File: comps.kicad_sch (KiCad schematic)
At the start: 9 parts, among them J3 Micro_SD_Card_Det, U7 ICM-20608-G, U8 MMC5983MA

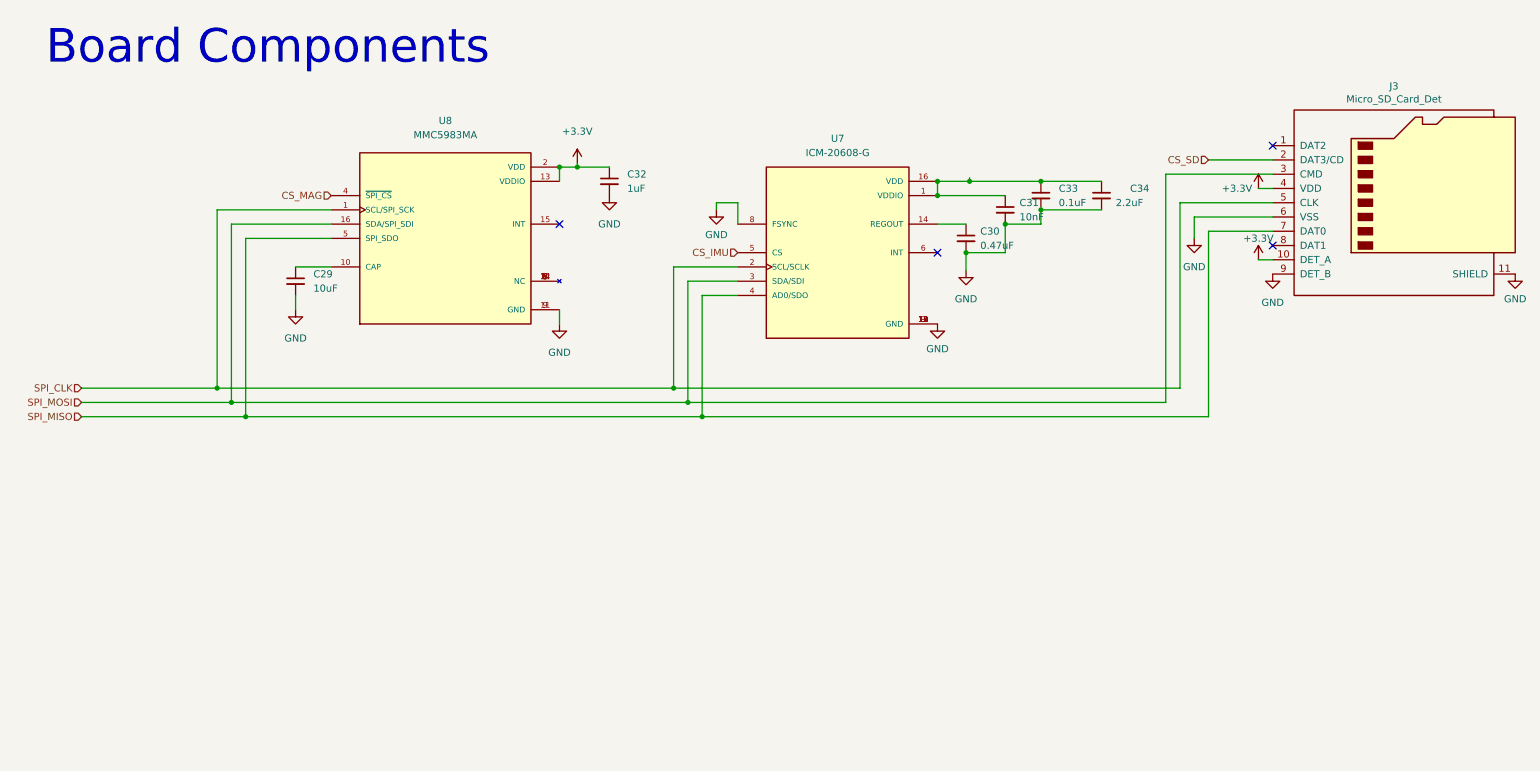
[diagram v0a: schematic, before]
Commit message: schematic review updated
fixed:
-pin 1 on the bootjumper is missing a connection. 
- Move the SD card to a 2nd SPI bus (so a 2nd set of MISO, MOSI, SCLK) as the rest of the bus is blocked while data is written to it, which would interrupt sensor readings. 
- Add a pull-up resistor on the DET_A pin of the micro SD card, and also connect that pin to the esp32 (picture from pickle) 
- VDD on the IMU (U7) is not connected to any power, should be connected to 3.3V 
- Turns out CAN capacitors C18, C19 actually aren’t needed. It’s up to you if you want to keep them, but if you do keep them could you change their value to “DNP” (stands for Do not place) 
-  Add test points to lines which can potentially cause issues. Most of the time this just means places that are connected to the ESP32, but especially places like the SPI lines (including chip selects). Also, add test points to TXD and RXD on the esp32 in case we have to solder to them for programming  

Servo Buck Converter 
- Pin 29 missing ground connection 
-  Add a text label with the part number of the 2.1uH inductor 

LTC4412s 
- No power net connected to Vin 
- stocky diodes replaced logic mosfets
- switched mosfets around so S is common
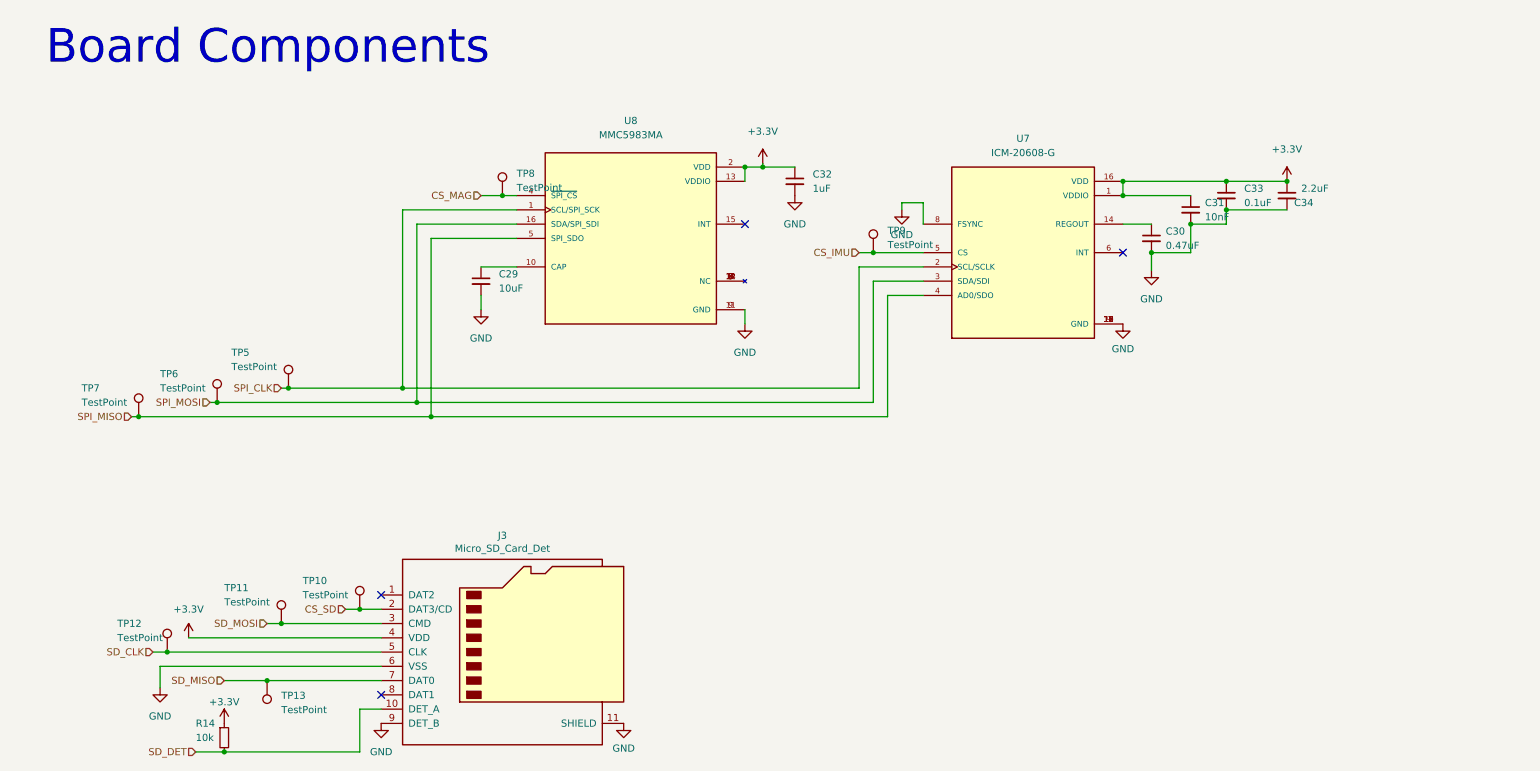
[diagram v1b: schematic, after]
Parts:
- added R14: 10k, symbol Device:R_Small
- added TP10, TP11, TP12, TP13, TP5, TP6, TP7, TP8, TP9: TestPoint, symbol Connector:TestPoint
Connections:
- net +3V3: now also C31.1, C33.1, C34.1, U7.1 (VDDIO), U7.16 (VDD), R14.1; no longer J3.10 (DET_A)
- net CS_IMU: now also TP9.1
- net CS_MAG: now also TP8.1
- net CS_SD: now also TP10.1
- net SPI_CLK: now also TP5.1; no longer J3.5 (CLK)
- net SPI_MISO: now also TP7.1; no longer J3.7 (DAT0)
- net SPI_MOSI: now also TP6.1; no longer J3.3 (CMD)
- new net SD_CLK: J3.5 (CLK), TP12.1
- new net SD_DET: J3.10 (DET_A), R14.2
- new net SD_MISO: J3.7 (DAT0), TP13.1
- new net SD_MOSI: J3.3 (CMD), TP11.1
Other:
- moved on the sheet: C29, C30, C31, C32, C33, C34, J3, U7, U8

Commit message: I don't want to lose all my changes so I will commit, commit.
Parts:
- R14: footprint (none) -> Resistor_SMD:R_0402_1005Metric
- TP10, TP11, TP12, TP13, TP5, TP6, TP7, TP8, TP9: footprint (none) -> TestPoint:TestPoint_Pad_D1.0mm
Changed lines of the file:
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@@
       (effects (font (size 1.27 1.27)) (justify left))
     )
-    (property "Footprint" "" (at 44.45 127 0)
+    (property "Footprint" "TestPoint:TestPoint_Pad_D1.0mm" (at 44.45 127 0)
       (effects (font (size 1.27 1.27)) hide)
     )
@@
       (effects (font (size 1.27 1.27)) (justify right))
     )
-    (property "Footprint" "" (at 52.07 132.08 0)
+    (property "Footprint" "TestPoint:TestPoint_Pad_D1.0mm" (at 52.07 132.08 0)
       (effects (font (size 1.27 1.27)) hide)
     )
@@
       (effects (font (size 1.27 1.27)) (justify left))
     )
-    (property "Footprint" "" (at 78.74 119.38 0)
+    (property "Footprint" "TestPoint:TestPoint_Pad_D1.0mm" (at 78.74 119.38 0)
       (effects (font (size 1.27 1.27)) hide)
     )
@@
       (effects (font (size 1.27 1.27)) (justify left))
     )
-    (property "Footprint" "" (at 104.14 45.72 0)
+    (property "Footprint" "TestPoint:TestPoint_Pad_D1.0mm" (at 104.14 45.72 0)
       (effects (font (size 1.27 1.27)) hide)
     )
@@
       (effects (font (size 1.27 1.27)) (justify left))
     )
-    (property "Footprint" "" (at 49.53 142.24 0)
+    (property "Footprint" "Resistor_SMD:R_0402_1005Metric" (at 49.53 142.24 0)
       (effects (font (size 1.27 1.27)) hide)
     )
@@
       (effects (font (size 1.27 1.27)) (justify left))
     )
-    (property "Footprint" "" (at 170.18 55.88 0)
+    (property "Footprint" "TestPoint:TestPoint_Pad_D1.0mm" (at 170.18 55.88 0)
       (effects (font (size 1.27 1.27)) hide)
     )
@@
       (effects (font (size 1.27 1.27)) (justify left))
     )
-    (property "Footprint" "" (at 39.37 85.09 0)
+    (property "Footprint" "TestPoint:TestPoint_Pad_D1.0mm" (at 39.37 85.09 0)
       (effects (font (size 1.27 1.27)) hide)
     )
@@
       (effects (font (size 1.27 1.27)) (justify left))
     )
-    (property "Footprint" "" (at 64.77 121.92 0)
+    (property "Footprint" "TestPoint:TestPoint_Pad_D1.0mm" (at 64.77 121.92 0)
       (effects (font (size 1.27 1.27)) hide)
     )
@@
       (effects (font (size 1.27 1.27)) (justify left))
     )
-    (property "Footprint" "" (at 53.34 82.55 0)
+    (property "Footprint" "TestPoint:TestPoint_Pad_D1.0mm" (at 53.34 82.55 0)
       (effects (font (size 1.27 1.27)) hide)
     )
@@
       (effects (font (size 1.27 1.27)) (justify left))
     )
-    (property "Footprint" "" (at 66.04 80.01 0)
-      (effects (font (size 1.27 1.27)) hide)
-    )
+    (property "Footprint" "TestPoint:TestPoint_Pad_D1.0mm" (at 66.04 80.01 0)
+      (effects (font (size 1.27 1.27)) hide)
+    )

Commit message: everything should be fine
fixed all mask stuff
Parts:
- added C23: 1uF, Capacitor_SMD:C_0402_1005Metric, symbol Device:C_Small
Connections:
- net +3V3: now also C23.2
- net GND: now also C23.1
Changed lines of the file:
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@@
   (junction (at 59.69 121.92) (diameter 0) (color 0 0 0 0)
+  )
+  (junction (at 45.72 124.46) (diameter 0) (color 0 0 0 0)
   )
   (junction (at 73.66 119.38) (diameter 0) (color 0 0 0 0)
@@
     (stroke (width 0) (type default))
   )
-  (wire (pts (xy 43.18 124.46) (xy 77.47 124.46))
+  (wire (pts (xy 43.18 124.46) (xy 45.72 124.46))
     (stroke (width 0) (type default))
   )
@@
   )
   (wire (pts (xy 165.1 82.55) (xy 165.1 60.96))
+    (stroke (width 0) (type default))
+  )
+  (wire (pts (xy 45.72 124.46) (xy 77.47 124.46))
     (stroke (width 0) (type default))
   )
@@
     )
   )
+  (symbol (lib_id "Device:C_Small") (at 45.72 121.92 0) (unit 1)
+    (in_bom yes) (on_board yes) (dnp no) (fields_autoplaced)
+    (property "Reference" "C23" (at 48.895 120.6562 0)
+      (effects (font (size 1.27 1.27)) (justify left))
+    )
+    (property "Value" "1uF" (at 48.895 123.1962 0)
+      (effects (font (size 1.27 1.27)) (justify left))
+    )
+    (property "Footprint" "Capacitor_SMD:C_0402_1005Metric" (at 45.72 121.92 0)
+      (effects (font (size 1.27 1.27)) hide)
+    )
+    (property "Datasheet" "~" (at 45.72 121.92 0)
+      (effects (font (size 1.27 1.27)) hide)
+    )
+    (pin "1")
+    (pin "2")
+    (instances
+      (project "Canardboard"
+        (path "/7db990e4-92e1-4f99-b4d2-435bbec1ba83/e0402675-af14-46ad-ab53-2a6080ba54c9"
+          (reference "C23") (unit 1)
+        )
+      )
+    )
+  )
   (symbol (lib_id "Connector:TestPoint") (at 57.15 132.08 180) (unit 1)
     (in_bom yes) (on_board yes) (dnp no) (fields_autoplaced)
@@
         )
       )
+    )
+  )
+  (symbol (lib_id "power:GND") (at 45.72 119.38 180) (unit 1)
+    (in_bom yes) (on_board yes) (dnp no) (fields_autoplaced)
+    (property "Reference" "#PWR084" (at 45.72 113.03 0)
+      (effects (font (size 1.27 1.27)) hide)
+    )
+    (property "Value" "GND" (at 45.72 115.57 0)
+      (effects (font (size 1.27 1.27)))
+    )
+    (property "Footprint" "" (at 45.72 119.38 0)
+      (effects (font (size 1.27 1.27)) hide)
+    )
+    (property "Datasheet" "" (at 45.72 119.38 0)
+      (effects (font (size 1.27 1.27)) hide)
+    )
+    (pin "1")
+    (instances
+      (project "Canardboard"
+        (path "/7db990e4-92e1-4f99-b4d2-435bbec1ba83/e0402675-af14-46ad-ab53-2a6080ba54c9"
+          (reference "#PWR084") (unit 1)
+        )
+      )
